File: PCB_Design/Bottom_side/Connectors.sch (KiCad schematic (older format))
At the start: 4 parts

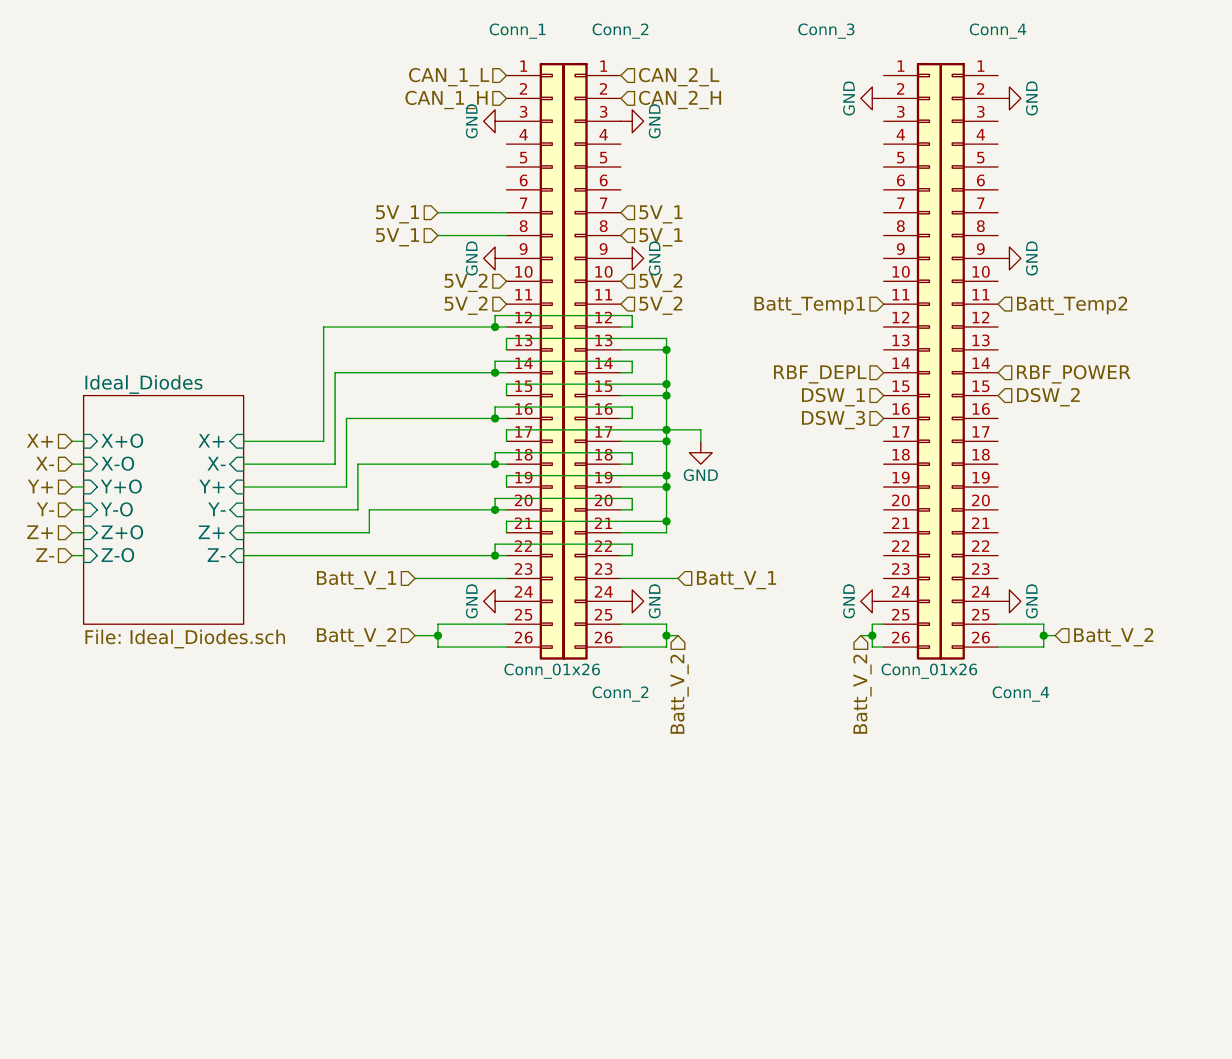
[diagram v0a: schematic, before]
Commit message: PCB bottom layer populated
PCB bottom layer populated, and waiting for top layer to be merged.
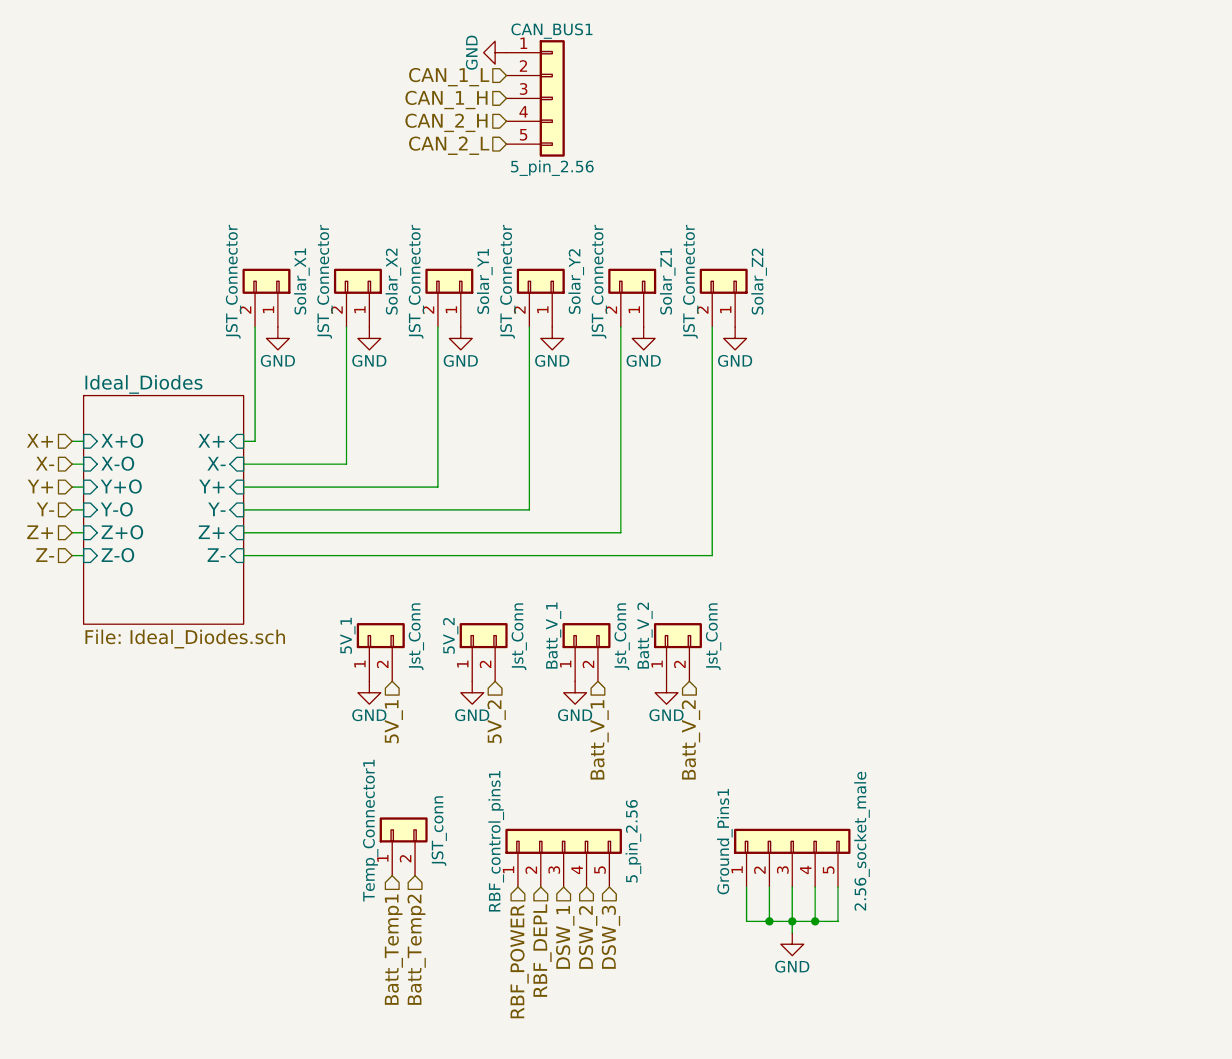
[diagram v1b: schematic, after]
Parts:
- removed Conn_1, Conn_3: Conn_01x26, Socket_Strips:Socket_Strip_Straight_1x26_Pitch2.54mm, symbol Conn_01x26
- removed Conn_2: Conn_2, Socket_Strips:Socket_Strip_Straight_1x26_Pitch2.54mm, symbol Conn_01x26
- removed Conn_4: Conn_4, Socket_Strips:Socket_Strip_Straight_1x26_Pitch2.54mm, symbol Conn_01x26
- added 5V_1, 5V_2, Batt_V_1, Batt_V_2: Jst_Conn, Connectors_JST:JST_XH_B02B-XH-A_02x2.50mm_Straight, symbol Conn_01x02
- added CAN_BUS1, RBF_control_pins1: 5_pin_2.56, Socket_Strips:Socket_Strip_Straight_1x05_Pitch2.54mm, symbol Conn_01x05
- added Ground_Pins1: 2.56_socket_male, Socket_Strips:Socket_Strip_Straight_1x05_Pitch2.54mm, symbol Conn_01x05
- added Solar_X1, Solar_X2, Solar_Y1, Solar_Y2, Solar_Z1, Solar_Z2: JST_Connector, Connectors_JST:JST_XH_B02B-XH-A_02x2.50mm_Straight, symbol Conn_01x02
- added Temp_Connector1: JST_conn, Connectors_JST:JST_XH_B02B-XH-A_02x2.50mm_Straight, symbol Conn_01x02
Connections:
- net 5V_1: now also 5V_1.2 (Pin_2)
- net 5V_2: now also 5V_2.2 (Pin_2)
- net Batt_Temp1: now also Temp_Connector1.1 (Pin_1)
- net Batt_Temp2: now also Temp_Connector1.2 (Pin_2)
- net Batt_V_1: now also Batt_V_1.2 (Pin_2)
- net Batt_V_2: now also Batt_V_2.2 (Pin_2)
- net CAN_1_H: now also CAN_BUS1.3 (Pin_3)
- net CAN_1_L: now also CAN_BUS1.2 (Pin_2)
- net CAN_2_H: now also CAN_BUS1.4 (Pin_4)
- net CAN_2_L: now also CAN_BUS1.5 (Pin_5)
- net DSW_1: now also RBF_control_pins1.3 (Pin_3)
- net DSW_2: now also RBF_control_pins1.4 (Pin_4)
- net DSW_3: now also RBF_control_pins1.5 (Pin_5)
- net GND: now also 5V_1.1 (Pin_1), 5V_2.1 (Pin_1), Batt_V_1.1 (Pin_1), Batt_V_2.1 (Pin_1), CAN_BUS1.1 (Pin_1), Ground_Pins1.1 (Pin_1), Ground_Pins1.2 (Pin_2), Ground_Pins1.3 (Pin_3), Ground_Pins1.4 (Pin_4), Ground_Pins1.5 (Pin_5), Solar_X1.1 (Pin_1), Solar_X2.1 (Pin_1), Solar_Y1.1 (Pin_1), Solar_Y2.1 (Pin_1), Solar_Z1.1 (Pin_1), Solar_Z2.1 (Pin_1)
- net Ideal_Diodes/X+: now also Solar_X1.2 (Pin_2)
- net Ideal_Diodes/X-: now also Solar_X2.2 (Pin_2)
- net Ideal_Diodes/Y+: now also Solar_Y1.2 (Pin_2)
- net Ideal_Diodes/Y-: now also Solar_Y2.2 (Pin_2)
- net Ideal_Diodes/Z+: now also Solar_Z1.2 (Pin_2)
- net Ideal_Diodes/Z-: now also Solar_Z2.2 (Pin_2)
- net RBF_DEPL: now also RBF_control_pins1.2 (Pin_2)
- net RBF_POWER: now also RBF_control_pins1.1 (Pin_1)

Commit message: Updated PCB structure tree
Full_PCB now includes bottom and top layer hierarchical sheets
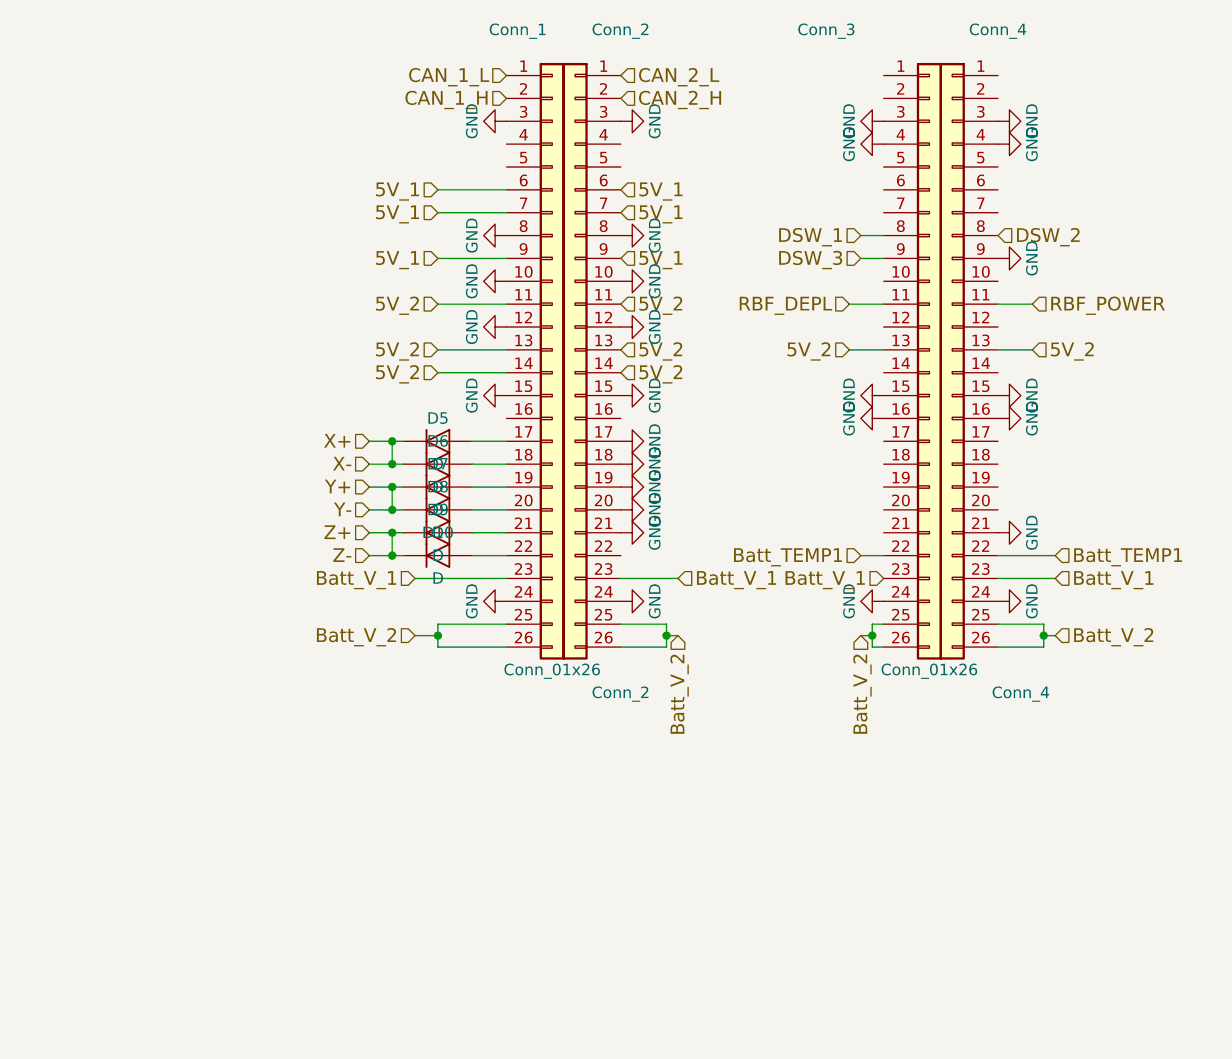
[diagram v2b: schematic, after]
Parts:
- removed 5V_1, 5V_2, Batt_V_1, Batt_V_2: Jst_Conn, Connectors_JST:JST_XH_B02B-XH-A_02x2.50mm_Straight, symbol Conn_01x02
- removed CAN_BUS1, RBF_control_pins1: 5_pin_2.56, Socket_Strips:Socket_Strip_Straight_1x05_Pitch2.54mm, symbol Conn_01x05
- removed Ground_Pins1: 2.56_socket_male, Socket_Strips:Socket_Strip_Straight_1x05_Pitch2.54mm, symbol Conn_01x05
- removed Solar_X1, Solar_X2, Solar_Y1, Solar_Y2, Solar_Z1, Solar_Z2: JST_Connector, Connectors_JST:JST_XH_B02B-XH-A_02x2.50mm_Straight, symbol Conn_01x02
- removed Temp_Connector1: JST_conn, Connectors_JST:JST_XH_B02B-XH-A_02x2.50mm_Straight, symbol Conn_01x02
- added Conn_1, Conn_3: Conn_01x26, Socket_Strips:Socket_Strip_Straight_1x26_Pitch2.54mm, symbol Conn_01x26
- added Conn_2: Conn_2, Socket_Strips:Socket_Strip_Straight_1x26_Pitch2.54mm, symbol Conn_01x26
- added Conn_4: Conn_4, Socket_Strips:Socket_Strip_Straight_1x26_Pitch2.54mm, symbol Conn_01x26
- added D10, D5, D6, D7, D8, D9: D, Diodes_SMD:D_SMA, symbol D
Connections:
- net 5V_1: now also Conn_1.6 (Pin_6), Conn_1.7 (Pin_7), Conn_1.9 (Pin_9), Conn_2.6 (Pin_6), Conn_2.7 (Pin_7), Conn_2.9 (Pin_9)
- net 5V_2: now also Conn_1.11 (Pin_11), Conn_1.13 (Pin_13), Conn_1.14 (Pin_14), Conn_2.11 (Pin_11), Conn_2.13 (Pin_13), Conn_2.14 (Pin_14), Conn_3.13 (Pin_13), Conn_4.13 (Pin_13)
- net Batt_V_1: now also Conn_1.23 (Pin_23), Conn_2.23 (Pin_23), Conn_3.23 (Pin_23), Conn_4.23 (Pin_23)
- net Batt_V_2: now also Conn_1.25 (Pin_25), Conn_1.26 (Pin_26), Conn_2.25 (Pin_25), Conn_2.26 (Pin_26), Conn_3.25 (Pin_25), Conn_3.26 (Pin_26), Conn_4.25 (Pin_25), Conn_4.26 (Pin_26)
- net CAN_1_H: now also Conn_1.2 (Pin_2)
- net CAN_1_L: now also Conn_1.1 (Pin_1)
- net CAN_2_H: now also Conn_2.2 (Pin_2)
- net CAN_2_L: now also Conn_2.1 (Pin_1)
- net DSW_1: now also Conn_3.8 (Pin_8)
- net DSW_2: now also Conn_4.8 (Pin_8)
- net DSW_3: now also Conn_3.9 (Pin_9)
- net GND: now also Conn_1.10 (Pin_10), Conn_1.12 (Pin_12), Conn_1.15 (Pin_15), Conn_1.24 (Pin_24), Conn_1.3 (Pin_3), Conn_1.8 (Pin_8), Conn_2.10 (Pin_10), Conn_2.12 (Pin_12), Conn_2.15 (Pin_15), Conn_2.17 (Pin_17), Conn_2.18 (Pin_18), Conn_2.19 (Pin_19), Conn_2.20 (Pin_20), Conn_2.21 (Pin_21), Conn_2.24 (Pin_24), Conn_2.3 (Pin_3), Conn_2.8 (Pin_8), Conn_3.15 (Pin_15), Conn_3.16 (Pin_16), Conn_3.24 (Pin_24), Conn_3.3 (Pin_3), Conn_3.4 (Pin_4), Conn_4.15 (Pin_15), Conn_4.16 (Pin_16), Conn_4.21 (Pin_21), Conn_4.24 (Pin_24), Conn_4.3 (Pin_3), Conn_4.4 (Pin_4), Conn_4.9 (Pin_9)
- net RBF_DEPL: now also Conn_3.11 (Pin_11)
- net RBF_POWER: now also Conn_4.11 (Pin_11)
- net X+: now also D5.1 (K), D6.1 (K)
- net Y+: now also D7.1 (K), D8.1 (K)
- net Z+: now also D10.1 (K), D9.1 (K)
- new net: Conn_1.17 (Pin_17), D5.2 (A)
- new net: Conn_1.18 (Pin_18), D6.2 (A)
- new net: Conn_1.19 (Pin_19), D7.2 (A)
- new net: Conn_1.20 (Pin_20), D8.2 (A)
- new net: Conn_1.21 (Pin_21), D9.2 (A)
- new net: Conn_1.22 (Pin_22), D10.2 (A)
- new net Batt_TEMP1: Conn_3.22 (Pin_22), Conn_4.22 (Pin_22)
